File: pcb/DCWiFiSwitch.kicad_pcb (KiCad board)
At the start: 2 copper layers, 50 x 50 mm, 44 parts, among them J1 Screw_Terminal_01x06, J4 Prog, Q1 AO3400A, Q2 AO3400A, U1 TPS5430DDA, U2 ESP-12F, U3 EL817, U4 EL817

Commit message: board rc2
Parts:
- removed the H3 at (95.0, 45.0)
- removed the H4 at (95.0, 85.0)
- removed J4: Prog, Connector_PinHeader_2.54mm:PinHeader_1x05_P2.54mm_Vertical
- added H1: MH, MountingHole:MountingHole_3.2mm_M3_ISO7380, F.Cu at (95.0, 45.0)
- added H2: MH, MountingHole:MountingHole_3.2mm_M3_ISO7380, F.Cu at (95.0, 85.0)
- added J2: Conn_01x06, Connector_PinHeader_2.54mm:PinHeader_1x06_P2.54mm_Vertical, F.Cu at (101.7, 87.5)
- added R10: 10k, Resistor_SMD:R_0603_1608Metric, F.Cu at (118.0, 86.5)
- added R5: 10k, Resistor_SMD:R_0603_1608Metric, F.Cu at (118.0, 68.5)
- renumbered D3 to D1, D4 to D2, D5 to D3, D6 to D4, D1 to D5, D2 to D6, F2 to F1, F3 to F2, F1 to F3, H1 to H3, H2 to H4, R9 to R1, R1 to R11, R2 to R12, R3 to R13, R4 to R14, R5 to R15, R6 to R16, R7 to R17, R8 to R18, R10 to R2, R11 to R3, R12 to R4, R13 to R6, R14 to R7, R15 to R8, R16 to R9, U3 to U1, U4 to U2, U1 to U3, U2 to U4
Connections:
- U4 pad 2: unconnected-(U2-ADC-Pad2) -> ADC
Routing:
- net ADC: track 0.00 -> 15.3 mm
- net GND: track 21.6 -> 34.9 mm, vias 37 -> 38
- net NRST: track 26.0 -> 38.5 mm
- net RXD: track 27.8 -> 40.1 mm
- net TXD: track 31.1 -> 39.8 mm
- net Net-(D4-A): track 3.17 -> 5.93 mm
- net Net-(D2-A): track 3.17 -> 5.93 mm
- net Net-(Q2-G): track 22.0 -> 23.5 mm
- net Net-(Q1-G): track 22.1 -> 23.5 mm
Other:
- outline, holes or cut-outs redrawn
- board text added: "12-24V"
- board text added: "ADC"
- board text added: "DC WiFi Switch Tomas Barak 2024"
- board text added: "EN"
- board text added: "GND"
- board text added: "JLCJLCJLCJLC"
- board text added: "NRST"
- board text added: "OUT1+"
- board text added: "OUT1-"
- board text added: "OUT2+"
- board text added: "OUT2-"
- board text added: "RXD"
- board text added: "TXD"

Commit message: board rc3
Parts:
- R14: renamed from R10; value 10k -> 5k6
- R9: renamed from R5; value 10k -> 5k6
- renumbered D5 to D1, D6 to D2, D1 to D3, D2 to D4, D3 to D5, D4 to D6, F3 to F1, F1 to F2, F2 to F3, R11 to R1, R6 to R10, R7 to R11, R8 to R12, R9 to R13, R12 to R2, R13 to R3, R14 to R4, R1 to R5, R2 to R6, R3 to R7, R4 to R8, U3 to U1, U1 to U2, U2 to U3
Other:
- board text added: "2x3A inductive"
- board text added: "50x50mm 40x40mm M3"
- board text added: "ESP-12F"

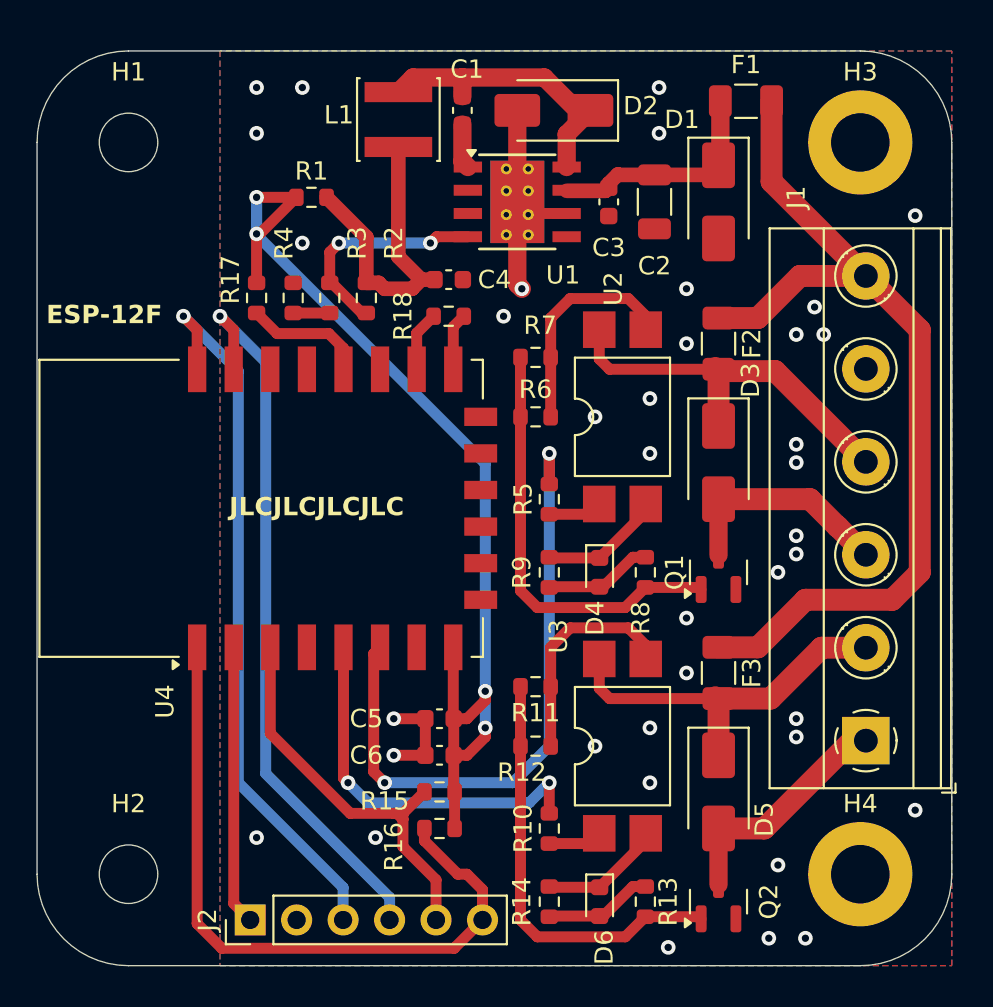
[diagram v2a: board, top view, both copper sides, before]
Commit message: fixed gpio programmer, board rc4
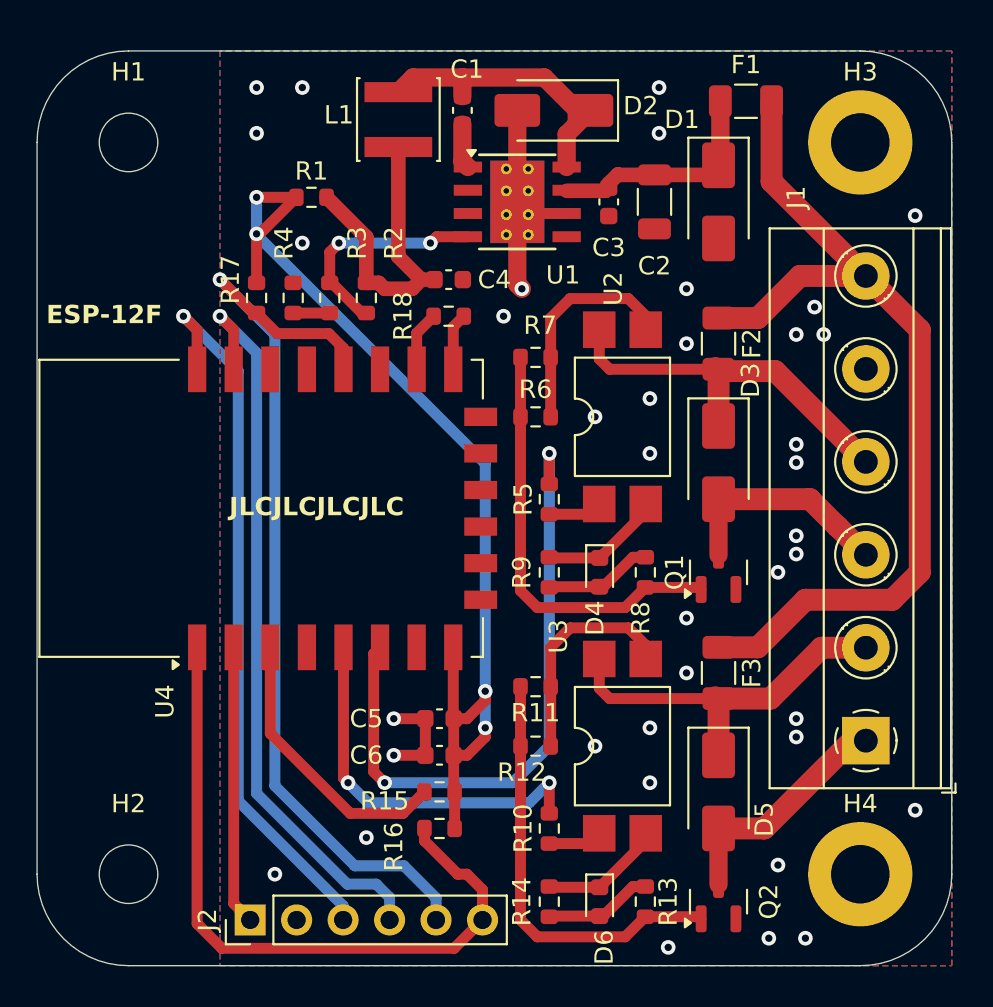
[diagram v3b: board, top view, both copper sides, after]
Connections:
- J2 pad 5: EN -> BOOT
- R15 pad 1: EN -> Net-(U4-EN)
- R17 pad 1: Net-(U4-GPIO0) -> BOOT
- U4 pad 18: Net-(U4-GPIO0) -> BOOT
- U4 pad 3: EN -> Net-(U4-EN)
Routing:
- net BOOT: track 0.00 -> 50.9 mm, vias 0 -> 1
- net EN: track 22.6 -> 0.00 mm
- net Net-(U4-EN): track 0.00 -> 15.6 mm
- net Net-(U4-GPIO0): track 6.70 -> 0.00 mm
- net RXD: track 40.1 -> 41.0 mm
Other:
- board text added: "BOOT"
- board text removed: "EN"
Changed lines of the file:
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@@
 	(net 6 "Net-(D1-K)")
 	(net 7 "TXD")
-	(net 8 "EN")
+	(net 8 "BOOT")
 	(net 9 "RXD")
 	(net 10 "NRST")
@@
 	(net 20 "CTRL2")
 	(net 21 "Net-(R11-Pad1)")
-	(net 22 "Net-(U4-GPIO0)")
+	(net 22 "Net-(U4-EN)")
 	(net 23 "Net-(U4-GPIO15)")
 	(net 24 "unconnected-(U1-NC-Pad2)")
@@
 			(layers "F.Cu" "F.Paste" "F.Mask")
 			(roundrect_rratio 0.25)
-			(net 22 "Net-(U4-GPIO0)")
+			(net 8 "BOOT")
 			(pintype "passive")
 		)
@@
 			(size 2.5 1)
 			(layers "F.Cu" "F.Paste" "F.Mask")
-			(net 8 "EN")
+			(net 22 "Net-(U4-EN)")
 			(pinfunction "EN")
 			(pintype "input")
@@
 			(size 2.5 1)
 			(layers "F.Cu" "F.Paste" "F.Mask")
-			(net 22 "Net-(U4-GPIO0)")
+			(net 8 "BOOT")
 			(pinfunction "GPIO0")
 			(pintype "bidirectional")
@@
 			(layers "F.Cu" "F.Paste" "F.Mask")
 			(roundrect_rratio 0.25)
-			(net 8 "EN")
+			(net 22 "Net-(U4-EN)")
 			(pintype "passive")
 		)
@@
 			(layers "*.Cu" "*.Mask")
 			(remove_unused_layers no)
-			(net 8 "EN")
+			(net 8 "BOOT")
 			(pinfunction "Pin_5")
 			(pintype "passive")
@@
 		)
 	)
-	(gr_text "EN"
-		(at 112.5 84 90)
+	(gr_text "BOOT"
+		(at 112.5 82.5 90)
 		(layer "B.SilkS")
 		(effects
@@
 	)
 	(via
-		(at 131.5 62.5)
+		(at 108 83)
 		(size 0.8)
 		(drill 0.4)
@@
 	)
 	(via
-		(at 138 81.5)
+		(at 103 85)
 		(size 0.8)
 		(drill 0.4)
@@
 	)
 	(via
-		(at 131.5 76.5)
+		(at 131.5 62.5)
 		(size 0.8)
 		(drill 0.4)
@@
 	)
 	(via
-		(at 130 88.5)
+		(at 138 81.5)
 		(size 0.8)
 		(drill 0.4)
@@
 	)
 	(via
-		(at 115.5 54.5)
+		(at 131.5 76.5)
 		(size 0.8)
 		(drill 0.4)
@@
 	)
 	(via
-		(at 102 83)
+		(at 130 88.5)
+		(size 0.8)
+		(drill 0.4)
+		(layers "F.Cu" "B.Cu")
+		(free yes)
+		(net 3)
+	)
+	(via
+		(at 115.5 54.5)
 		(size 0.8)
 		(drill 0.4)
@@
 	)
 	(via
-		(at 108.5 83)
-		(size 0.8)
-		(drill 0.4)
-		(layers "F.Cu" "B.Cu")
-		(free yes)
-		(net 3)
-	)
-	(via
 		(at 131.5 77.5)
 		(size 0.8)
@@
 	)
 	(segment
-		(start 101 80)
-		(end 106.73 85.73)
+		(start 98 54.5)
+		(end 101 57.5)
 		(width 0.6)
 		(layer "B.Cu")
@@
 	)
 	(segment
-		(start 98 54.5)
-		(end 101 57.5)
+		(start 106.73 86.73)
+		(end 106.73 87.5)
 		(width 0.6)
 		(layer "B.Cu")
@@
 	)
 	(segment
-		(start 101 57.5)
-		(end 101 80)
+		(start 101 81)
+		(end 106.73 86.73)
 		(width 0.6)
 		(layer "B.Cu")
@@
 	)
 	(segment
-		(start 106.73 85.73)
-		(end 106.73 87.5)
+		(start 101 57.5)
+		(end 101 81)
 		(width 0.6)
 		(layer "B.Cu")
@@
 	)
 	(segment
-		(start 102.75 72.6)
-		(end 102.75 77.305635)
+		(start 101.825 54.325)
+		(end 100 52.5)
 		(width 0.6)
 		(layer "F.Cu")
@@
 	)
 	(segment
-		(start 110 81.675)
-		(end 110 82)
+		(start 102 54.325)
+		(end 101.825 54.325)
 		(width 0.6)
 		(layer "F.Cu")
@@
 	)
 	(segment
-		(start 111.81 85.31)
-		(end 111.81 87.5)
+		(start 103.125 55.45)
+		(end 105.95 55.45)
 		(width 0.6)
 		(layer "F.Cu")
@@
 	)
 	(segment
-		(start 107.119365 81.675)
-		(end 109.5 81.675)
+		(start 106.75 56.25)
+		(end 106.75 57.4)
 		(width 0.6)
 		(layer "F.Cu")
@@
 	)
 	(segment
-		(start 111.175 80.5)
-		(end 110 81.675)
+		(start 102 54.325)
+		(end 103.125 55.45)
 		(width 0.6)
 		(layer "F.Cu")
@@
 	)
 	(segment
-		(start 109.5 81.675)
-		(end 109.675 81.675)
+		(start 105.95 55.45)
+		(end 106.75 56.25)
 		(width 0.6)
 		(layer "F.Cu")
 		(net 8)
 	)
+	(via
+		(at 100 52.5)
+		(size 0.8)
+		(drill 0.4)
+		(layers "F.Cu" "B.Cu")
+		(net 8)
+	)
 	(segment
-		(start 102.75 77.305635)
-		(end 107.119365 81.675)
+		(start 107.371321 84.542893)
+		(end 110.054974 84.542893)
 		(width 0.6)
-		(layer "F.Cu")
+		(layer "B.Cu")
 		(net 8)
 	)
 	(segment
-		(start 109.675 81.675)
-		(end 110 82)
+		(start 110.054974 84.542893)
+		(end 111.81 86.297919)
 		(width 0.6)
-		(layer "F.Cu")
+		(layer "B.Cu")
 		(net 8)
 	)
 	(segment
-		(start 110 82)
-		(end 110 83.5)
+		(start 103 80.171572)
+		(end 107.371321 84.542893)
 		(width 0.6)
-		(layer "F.Cu")
+		(layer "B.Cu")
 		(net 8)
 	)
 	(segment
-		(start 109.5 81.675)
-		(end 110 81.675)
+		(start 100 52.5)
+		(end 103 55.5)
 		(width 0.6)
-		(layer "F.Cu")
+		(layer "B.Cu")
 		(net 8)
 	)
 	(segment
-		(start 110 83.5)
-		(end 111.81 85.31)
+		(start 103 55.5)
+		(end 103 80.171572)
 		(width 0.6)
-		(layer "F.Cu")
+		(layer "B.Cu")
+		(net 8)
+	)
+	(segment
+		(start 111.81 86.297919)
+		(end 111.81 87.5)
+		(width 0.6)
+		(layer "B.Cu")
 		(net 8)
 	)
@@
 	)
 	(segment
-		(start 102.5 79.5)
-		(end 109.27 86.27)
+		(start 109.27 86.27)
+		(end 108.542893 85.542893)
 		(width 0.6)
 		(layer "B.Cu")
@@
 	)
 	(segment
-		(start 102.5 57)
-		(end 102.5 79.5)
+		(start 106.957107 85.542893)
+		(end 102 80.585786)
 		(width 0.6)
 		(layer "B.Cu")
@@
 	)
 	(segment
-		(start 100 54.5)
-		(end 102.5 57)
+		(start 102 80.585786)
+		(end 102 56.5)
 		(width 0.6)
 		(layer "B.Cu")
@@
 	)
 	(segment
-		(start 109.27 86.27)
-		(end 109.27 87.5)
+		(start 109.27 87.5)
+		(end 109.27 86.27)
+		(width 0.6)
+		(layer "B.Cu")
+		(net 9)
+	)
+	(segment
+		(start 102 56.5)
+		(end 100 54.5)
+		(width 0.6)
+		(layer "B.Cu")
+		(net 9)
+	)
+	(segment
+		(start 108.542893 85.542893)
+		(end 106.957107 85.542893)
 		(width 0.6)
 		(layer "B.Cu")
@@
 	)
 	(segment
-		(start 103.125 55.45)
-		(end 105.95 55.45)
+		(start 102.75 72.6)
+		(end 102.75 77.305635)
 		(width 0.6)
 		(layer "F.Cu")
@@
 	)
 	(segment
-		(start 106.75 56.25)
-		(end 106.75 57.4)
+		(start 107.119365 81.675)
+		(end 109.5 81.675)
 		(width 0.6)
 		(layer "F.Cu")
@@
 	)
 	(segment
-		(start 102 54.325)
-		(end 103.125 55.45)
+		(start 111.175 80.5)
+		(end 110 81.675)
 		(width 0.6)
 		(layer "F.Cu")
@@
 	)
 	(segment
-		(start 105.95 55.45)
-		(end 106.75 56.25)
+		(start 109.5 81.675)
+		(end 109.675 81.675)
+		(width 0.6)
+		(layer "F.Cu")
+		(net 22)
+	)
+	(segment
+		(start 102.75 77.305635)
+		(end 107.119365 81.675)
+		(width 0.6)
+		(layer "F.Cu")
+		(net 22)
+	)
+	(segment
+		(start 109.5 81.675)
+		(end 110 81.675)
 		(width 0.6)
 		(layer "F.Cu")

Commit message: added more silkscreen help and a push button, rc5
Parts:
- added SW1: SW1_BOOT, Button_Switch_SMD:SW_Push_1P1T_XKB_TS-1187A, F.Cu at (103.0, 45.0)
- moved R1 1.00 mm to (105.0, 49.0)
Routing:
- net BOOT: track 50.9 -> 64.0 mm
- net TXD: track 39.8 -> 33.4 mm
- net RXD: track 41.0 -> 34.6 mm
- net +3V3: track 59.9 -> 56.5 mm
- net GND: vias 38 -> 45
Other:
- board text added: "2x3A inductive GPIO12, GPIO14"
- board text added: "GPIO0 Boot UART"
- board text added: "github.com/barycz/DCWiFiSwitch dim: 50x50mm holes: 40x40mm, M3"
- board text removed: "2x3A inductive"
- board text removed: "50x50mm 40x40mm M3"
